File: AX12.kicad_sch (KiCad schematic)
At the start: 7 parts, among them J25 Conn_AX12, J29 Conn_AX12, U5 74LVC2G241

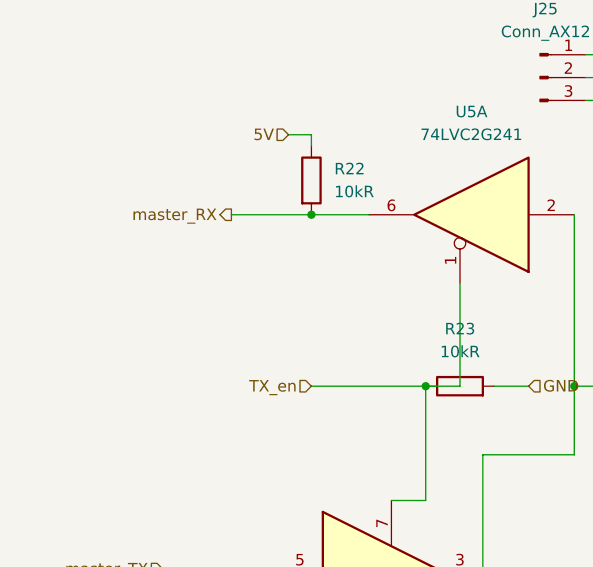
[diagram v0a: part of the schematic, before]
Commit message: fix 3.3V/5V compatibility + add 120Ohms + add I2C pullups
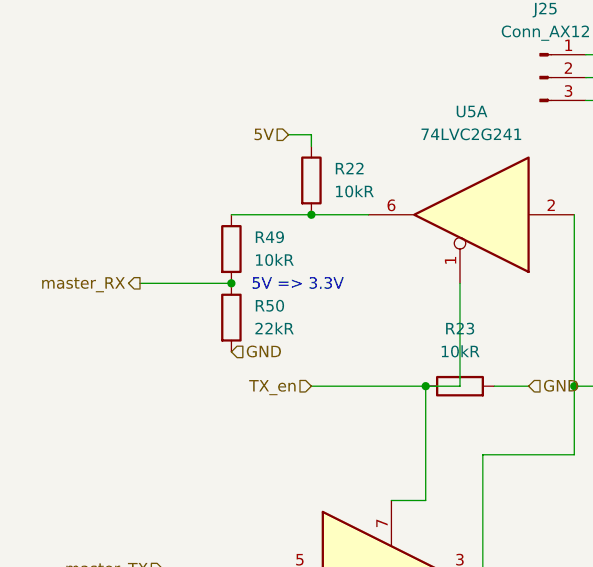
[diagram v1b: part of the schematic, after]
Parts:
- added R49: 10kR, Resistor_SMD:R_0603_1608Metric, symbol Device:R
- added R50: 22kR, Resistor_SMD:R_0603_1608Metric, symbol Device:R
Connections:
- net GND: now also R50.2
- net master_RX: now also R49.2, R50.1; no longer R22.2, U5.6
- new net: R22.2, R49.1, U5.6
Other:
- note added: "5V => 3.3V"
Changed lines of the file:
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@@
+	)
+	(junction
+		(at 69.85 91.44)
+		(diameter 0)
+		(color 0 0 0 0)
 	)
 	(junction
@@
 	(wire
 		(pts
+			(xy 59.69 91.44) (xy 69.85 91.44)
+		)
+		(stroke
+			(width 0)
+			(type default)
+		)
+	)
+	(wire
+		(pts
 			(xy 138.43 113.03) (xy 142.24 113.03)
 		)
@@
 			(width 0)
 			(type default)
+		)
+	)
+	(text "5V => 3.3V"
+		(exclude_from_sim no)
+		(at 77.216 91.694 0)
+		(effects
+			(font
+				(size 1.27 1.27)
+			)
 		)
 	)
@@
 		)
 	)
-	(hierarchical_label "5V"
-		(shape input)
-		(at 114.3 91.44 180)
-		(effects
-			(font
-				(size 1.27 1.27)
-			)
-			(justify right)
-		)
-	)
-	(hierarchical_label "12V"
-		(shape input)
-		(at 115.57 68.58 0)
-		(effects
-			(font
-				(size 1.27 1.27)
-			)
-			(justify left)
-		)
-	)
 	(hierarchical_label "master_RX"
 		(shape output)
-		(at 69.85 83.82 180)
+		(at 59.69 91.44 180)
 		(effects
 			(font
@@
 			)
 			(justify right)
+		)
+	)
+	(hierarchical_label "5V"
+		(shape input)
+		(at 114.3 91.44 180)
+		(effects
+			(font
+				(size 1.27 1.27)
+			)
+			(justify right)
+		)
+	)
+	(hierarchical_label "12V"
+		(shape input)
+		(at 115.57 68.58 0)
+		(effects
+			(font
+				(size 1.27 1.27)
+			)
+			(justify left)
+		)
+	)
+	(hierarchical_label "GND"
+		(shape input)
+		(at 69.85 99.06 0)
+		(effects
+			(font
+				(size 1.27 1.27)
+			)
+			(justify left)
 		)
 	)
@@
 	)
 	(symbol
+		(lib_id "Device:R")
+		(at 69.85 87.63 0)
+		(unit 1)
+		(exclude_from_sim no)
+		(in_bom yes)
+		(on_board yes)
+		(dnp no)
+		(fields_autoplaced yes)
+		(property "Reference" "R49"
+			(at 72.39 86.3599 0)
+			(effects
+				(font
+					(size 1.27 1.27)
+				)
+				(justify left)
+			)
+		)
+		(property "Value" "10kR"
+			(at 72.39 88.8999 0)
+			(effects
+				(font
+					(size 1.27 1.27)
+				)
+				(justify left)
+			)
+		)
+		(property "Footprint" "Resistor_SMD:R_0603_1608Metric"
+			(at 68.072 87.63 90)
+			(effects
+				(font
+					(size 1.27 1.27)
+				)
+				(hide yes)
+			)
+		)
+		(property "Datasheet" "~"
+			(at 69.85 87.63 0)
+			(effects
+				(font
+					(size 1.27 1.27)
+				)
+				(hide yes)
+			)
+		)
+		(property "Description" ""
+			(at 69.85 87.63 0)
+			(effects
+				(font
+					(size 1.27 1.27)
+				)
+				(hide yes)
+			)
+		)
+		(property "LCSC#" "C2930027"
+			(at 69.85 87.63 0)
+			(effects
+				(font
+					(size 1.27 1.27)
+				)
+				(hide yes)
+			)
+		)
+		(pin "1"
+		)
+		(pin "2"
+		)
+		(instances
+			(project "carte_servo"
+				(path "/e63e39d7-6ac0-4ffd-8aa3-1841a4541b55/66026453-9027-4575-bae8-7143b4848e55"
+					(reference "R49")
+					(unit 1)
+				)
+			)
+		)
+	)
+	(symbol
 		(lib_id "Connector:Conn_01x03_Pin")
 		(at 104.14 68.58 0)
@@
 					(unit 1)
 				)
+			)
+		)
+	)
+	(symbol
+		(lib_id "Device:R")
+		(at 69.85 95.25 0)
+		(unit 1)
+		(exclude_from_sim no)
+		(in_bom yes)
+		(on_board yes)
+		(dnp no)
+		(fields_autoplaced yes)
+		(property "Reference" "R50"
+			(at 72.39 93.9799 0)
+			(effects
+				(font
+					(size 1.27 1.27)
+				)
+				(justify left)
+			)
+		)
+		(property "Value" "22kR"
+			(at 72.39 96.5199 0)
+			(effects
+				(font
+					(size 1.27 1.27)
+				)
+				(justify left)
+			)
+		)
+		(property "Footprint" "Resistor_SMD:R_0603_1608Metric"
+			(at 68.072 95.25 90)
+			(effects
+				(font
+					(size 1.27 1.27)
+				)
+				(hide yes)
+			)
+		)
+		(property "Datasheet" "~"
+			(at 69.85 95.25 0)
+			(effects
+				(font
+					(size 1.27 1.27)
+				)
+				(hide yes)
+			)
+		)
+		(property "Description" ""
+			(at 69.85 95.25 0)
+			(effects
+				(font
+					(size 1.27 1.27)
+				)
+				(hide yes)
+			)
+		)
+		(property "LCSC#" "C2930027"
+			(at 69.85 95.25 0)
+			(effects
+				(font
+					(size 1.27 1.27)
+				)
+				(hide yes)
+			)
+		)
+		(pin "1"
+		)
+		(pin "2"
+		)
+		(instances
+			(project "carte_servo"
+				(path "/e63e39d7-6ac0-4ffd-8aa3-1841a4541b55/66026453-9027-4575-bae8-7143b4848e55"
+					(reference "R50")
+					(unit 1)
+				)

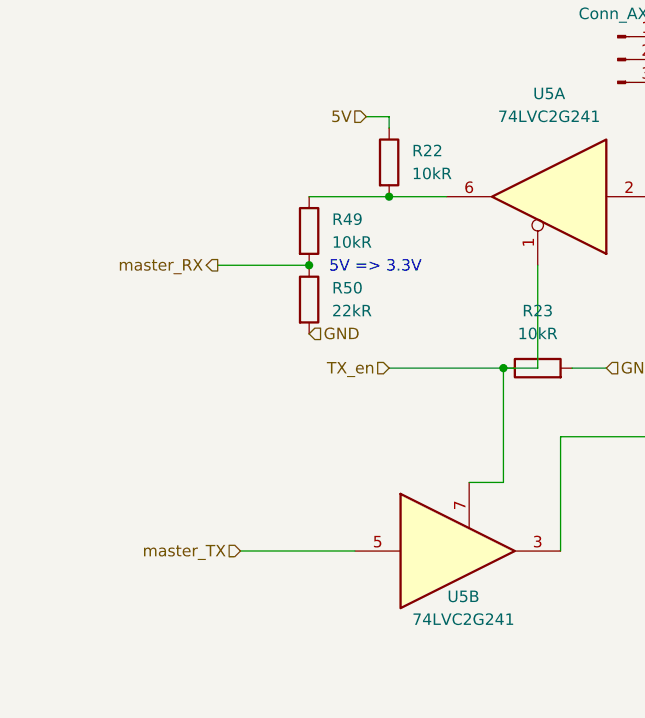
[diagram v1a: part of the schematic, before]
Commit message: Go to 3.3V + fix io_exp + routing
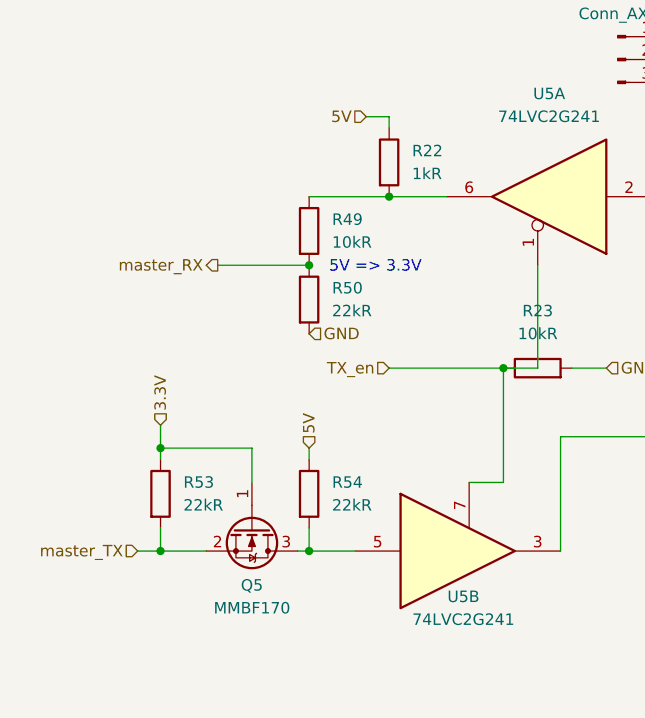
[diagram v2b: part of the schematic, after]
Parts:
- added Q5: MMBF170, Package_TO_SOT_SMD:SOT-23, symbol Transistor_FET:MMBF170
- added R53, R54: 22kR, Resistor_SMD:R_0603_1608Metric, symbol Device:R
- R22: value 10kR -> 1kR
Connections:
- net 5V: now also R54.1
- net master_TX: now also Q5.2 (S), R53.2; no longer U5.5
- new net: Q5.3 (D), R54.2, U5.5
- new net 3.3V: Q5.1 (G), R53.1

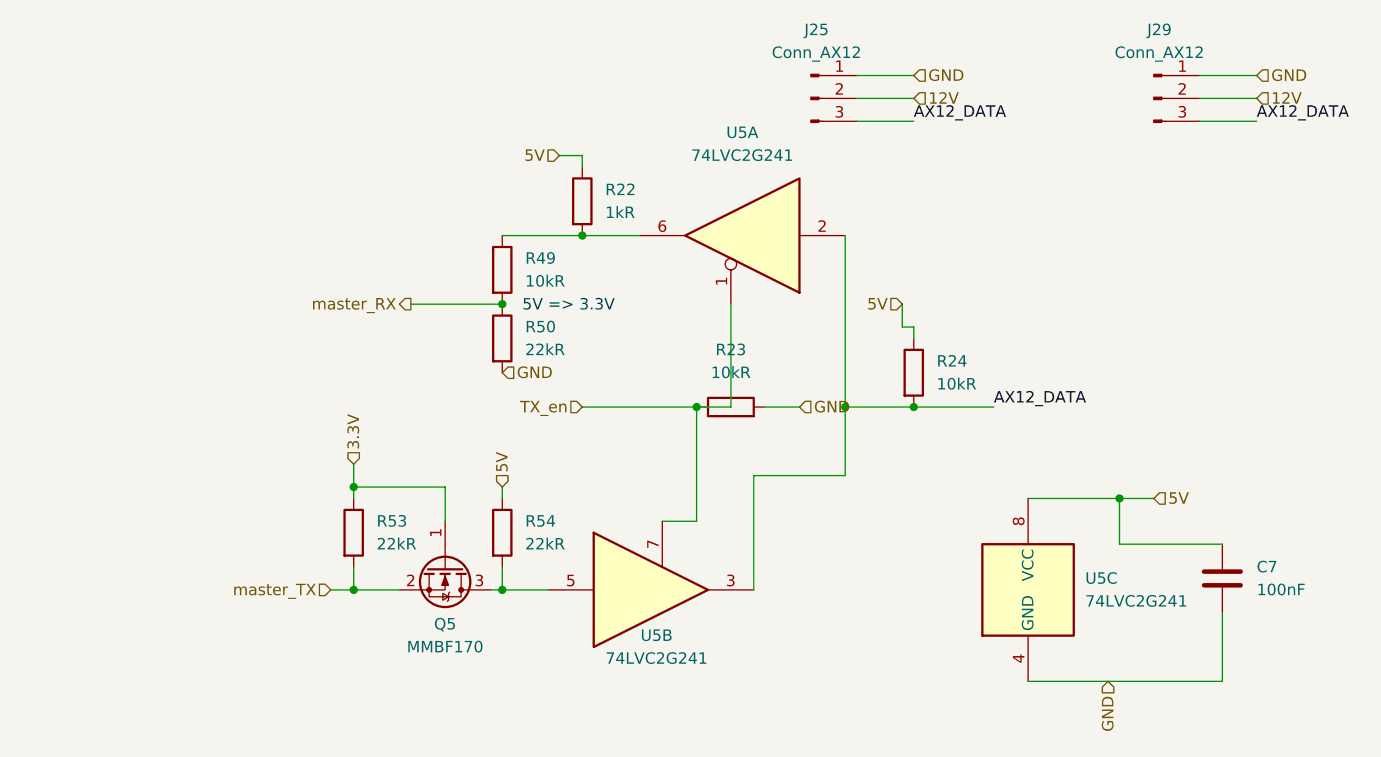
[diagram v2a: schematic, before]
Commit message: add 3.3V/5V conversion on AX12 RX/TX enable
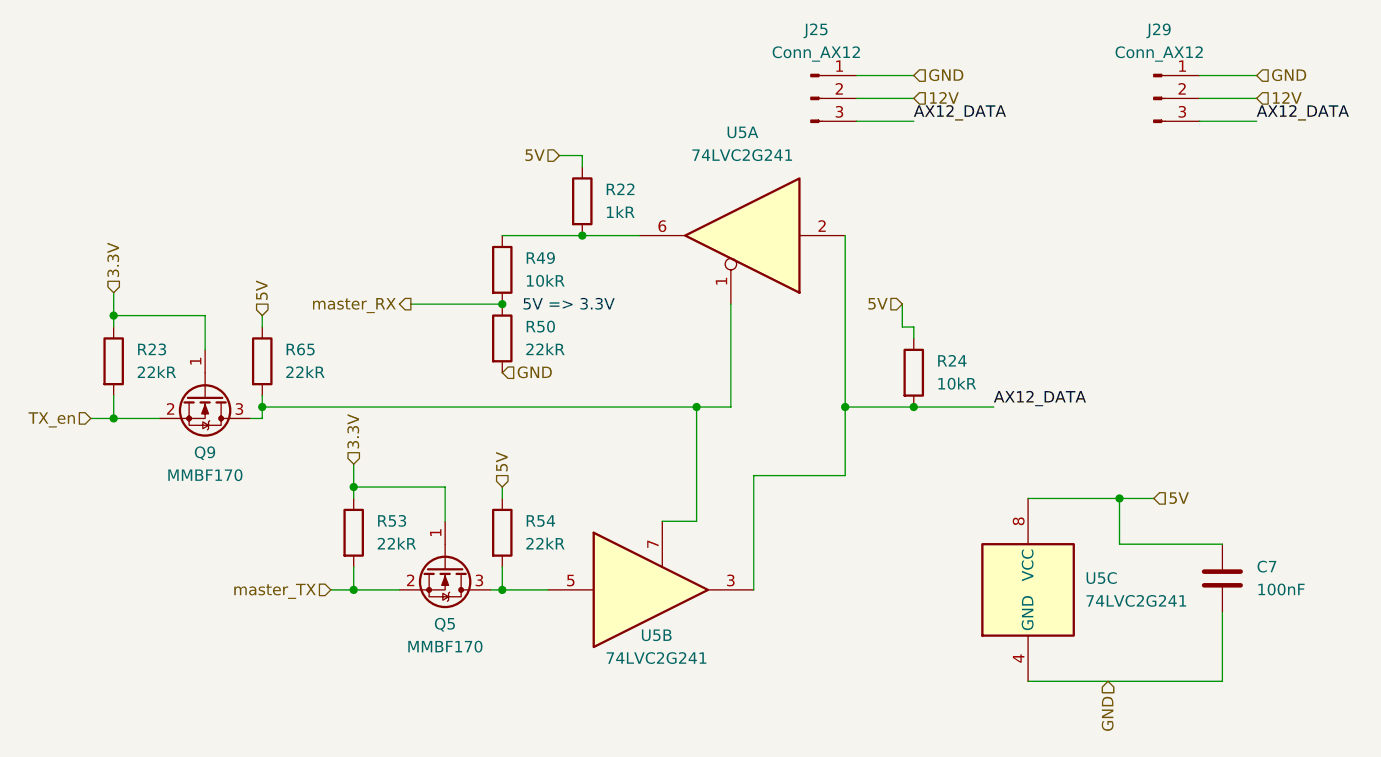
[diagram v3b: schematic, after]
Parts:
- added Q9: MMBF170, Package_TO_SOT_SMD:SOT-23, symbol Transistor_FET:MMBF170
- added R65: 22kR, Resistor_SMD:R_0603_1608Metric, symbol Device:R
- R23: value 10kR -> 22kR
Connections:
- net 3.3V: now also R23.1, Q9.1 (G)
- net 5V: now also R65.1
- net GND: no longer R23.2
- net TX_en: now also R23.2, Q9.2 (S); no longer R23.1, U5.1, U5.7
- new net: Q9.3 (D), R65.2, U5.1, U5.7

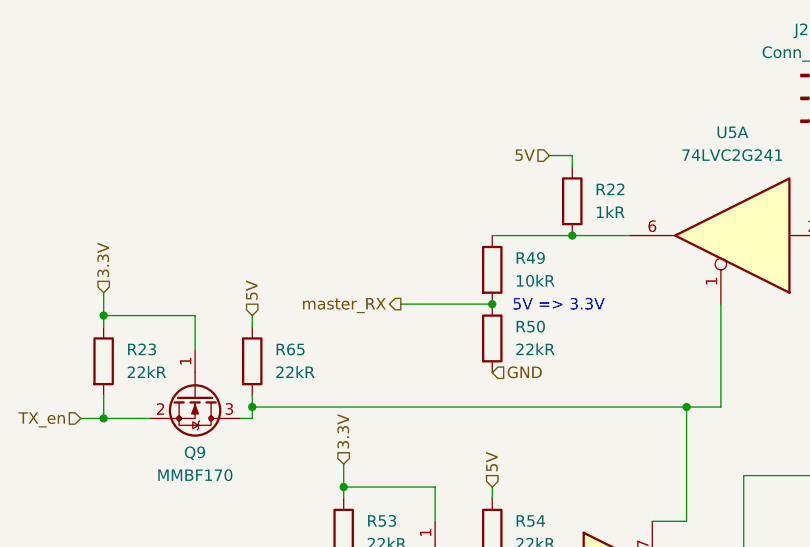
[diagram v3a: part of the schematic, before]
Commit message: fix AX12 RX: add proper 3.3V/5V level shifter
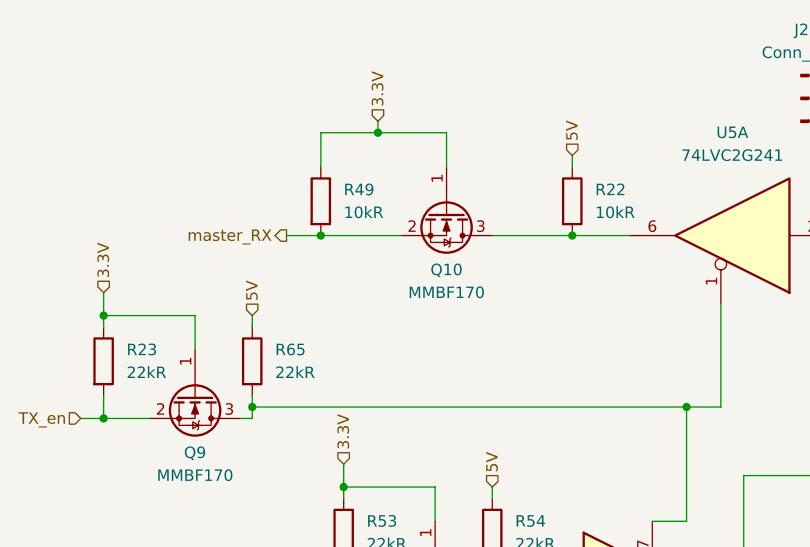
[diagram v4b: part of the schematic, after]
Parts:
- removed R50: 22kR, Resistor_SMD:R_0603_1608Metric, symbol Device:R
- added Q10: MMBF170, Package_TO_SOT_SMD:SOT-23, symbol Transistor_FET:MMBF170
- R22: value 1kR -> 10kR
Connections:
- net 3.3V: now also R49.1, Q10.1 (G)
- net master_RX: now also Q10.2 (S)
- net at R22.2, U5.6: now also Q10.3 (D); no longer R49.1
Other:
- note removed: "5V => 3.3V"

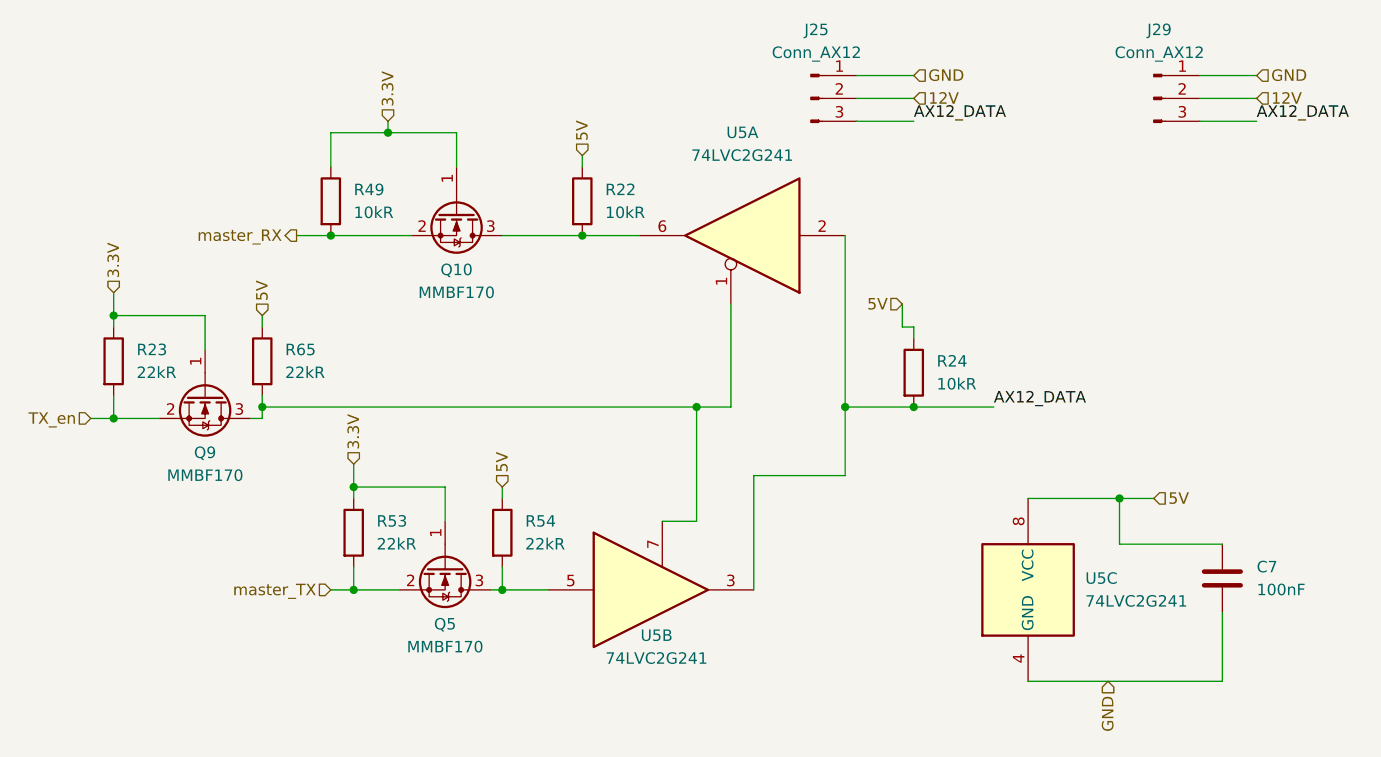
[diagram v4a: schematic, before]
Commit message: update to Kicad 9 + small fixes
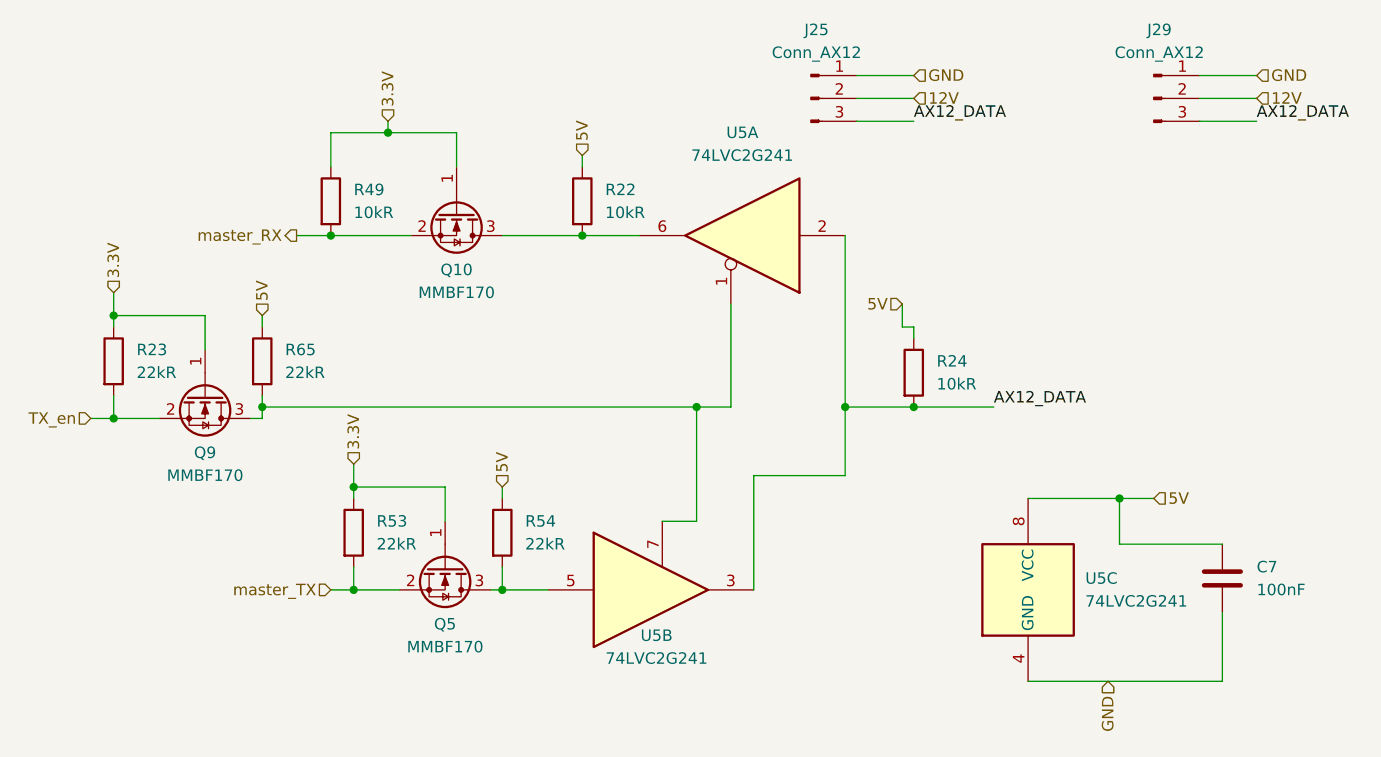
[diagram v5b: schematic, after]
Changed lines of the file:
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@@
 (kicad_sch
-	(version 20231120)
+	(version 20250114)
 	(generator "eeschema")
-	(generator_version "8.0")
+	(generator_version "9.0")
 	(paper "A4")
 	(junction
@@
 			)
 		)
-		(property "Description" ""
+		(property "Description" "Resistor"
 			(at 26.67 97.79 0)
 			(effects
@@
 			)
 		)
-		(property "Description" ""
+		(property "Description" "Resistor"
 			(at 78.74 80.01 0)
 			(effects
@@
 			)
 		)
-		(property "Description" ""
+		(property "Description" "Resistor"
 			(at 50.8 80.01 0)
 			(effects
@@
 			)
 		)
-		(property "Description" ""
+		(property "Description" "Resistor"
 			(at 69.85 116.84 0)
 			(effects
@@
 			)
 		)
-		(property "Description" ""
+		(property "Description" "Unpolarized capacitor"
 			(at 149.86 121.92 0)
 			(effects
@@
 	)
 	(symbol
-		(lib_name "74LVC2G241_1")
 		(lib_id "74xGxx:74LVC2G241")
 		(at 95.25 83.82 180)
@@
 			)
 		)
-		(property "Description" ""
+		(property "Description" "Resistor"
 			(at 43.18 97.79 0)
 			(effects
@@
 			)
 		)
-		(property "Description" ""
+		(property "Description" "Resistor"
 			(at 115.57 99.06 0)
 			(effects
@@
 			)
 		)
-		(property "Description" ""
+		(property "Description" "Resistor"
 			(at 53.34 116.84 0)
 			(effects

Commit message: update BOM
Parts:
- Q10, Q5, Q9: LCSC# (none) -> C28871
- R23, R53, R54, R65: LCSC# C2930027 -> C2907128
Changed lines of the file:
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@@
 			)
 		)
-		(property "LCSC#" "C2930027"
+		(property "LCSC#" "C2907128"
 			(at 26.67 97.79 0)
 			(effects
@@
 			)
 		)
+		(property "LCSC#" "C28871"
+			(at 64.77 81.28 90)
+			(effects
+				(font
+					(size 1.27 1.27)
+				)
+				(hide yes)
+			)
+		)
 		(pin "2"
 		)
@@
 			)
 		)
+		(property "LCSC#" "C28871"
+			(at 63.5 120.65 90)
+			(effects
+				(font
+					(size 1.27 1.27)
+				)
+				(hide yes)
+			)
+		)
 		(pin "2"
 		)
@@
 			)
 		)
-		(property "LCSC#" "C2930027"
+		(property "LCSC#" "C2907128"
 			(at 69.85 116.84 0)
 			(effects
@@
 			)
 		)
+		(property "LCSC#" "C28871"
+			(at 36.83 101.6 90)
+			(effects
+				(font
+					(size 1.27 1.27)
+				)
+				(hide yes)
+			)
+		)
 		(pin "2"
 		)
@@
 			)
 		)
-		(property "LCSC#" "C2930027"
+		(property "LCSC#" "C2907128"
 			(at 43.18 97.79 0)
 			(effects
@@
 			)
 		)
-		(property "LCSC#" "C2930027"
+		(property "LCSC#" "C2907128"
 			(at 53.34 116.84 0)
 			(effects
